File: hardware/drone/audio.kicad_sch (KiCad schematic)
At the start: 0 parts

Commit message: Worked on audio schematic (Codec, mic, d class audio amp, speaker)
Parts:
- added C66, C70, C71, C75, C76, C77: 100n, symbol Device:C
- added C67, C69, C72, C79: 10u, symbol Device:C
- added C68, C73, C74, C78: 1u, symbol Device:C
- added LS1: Speaker, symbol Device:Speaker
- added MK2: IM73A135V01, Sensor_Audio:Infineon_PG-LLGA-5-2, symbol Sensor_Audio:IM73A135V01
- added R10, R9: 150k, symbol Device:R
- added U11: TAC5111, Package_SO:SOIC-8_3.9x4.9mm_P1.27mm, symbol SoftDrone:TAC5111
- added U12: LM4670SD/NOPB, Package_TO_SOT_SMD:SOT-23-5, symbol SoftDrone:LM4670SD/NOPB
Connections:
- new net: C69.1, C70.1, U11.1 (DREG)
- new net: C73.2, U11.15 (IN1P)
- new net: C74.2, U11.16 (IN1M)
- new net: C76.1, U11.19 (OUT1P)
- new net: C77.2, U11.20 (OUT1M)
- new net: C68.1, U11.24 (VREF)
- new net: C76.2, R9.1
- new net: R9.2, U12.2 (-IN)
- new net: C73.1, MK2.1 (OUT+)
- new net: C77.1, R10.1
- new net: LS1.1, U12.8 (VO2)
- new net: LS1.2, U12.5 (VO1)
- new net: R10.2, U12.3 (+IN)
- new net: C74.1, MK2.3 (OUT-)
- new net GND: C66.2, C67.2, C68.2, C69.2, C70.2, C71.2, C72.2, C75.1, C78.2, C79.2, MK2.4 (GND), MK2.5 (GND), U11.13 (ADDR), U11.25 (VSS), U11.26 (VSS), U11.27 (VSS), U11.28 (VSS), U11.29 (VSS), U12.4 (GND), U12.6 (GND), U12.9 (EP)
- new net VDD1V8: C71.1, C72.1, U11.6 (IOVDD)
- new net VDD2V75: C75.2, MK2.2 (V_{DD})
- new net VDD3V3: C66.1, C67.1, U11.23 (AVDD)
- new net VSYS_5V: C78.1, C79.1, U12.7 (VDD)

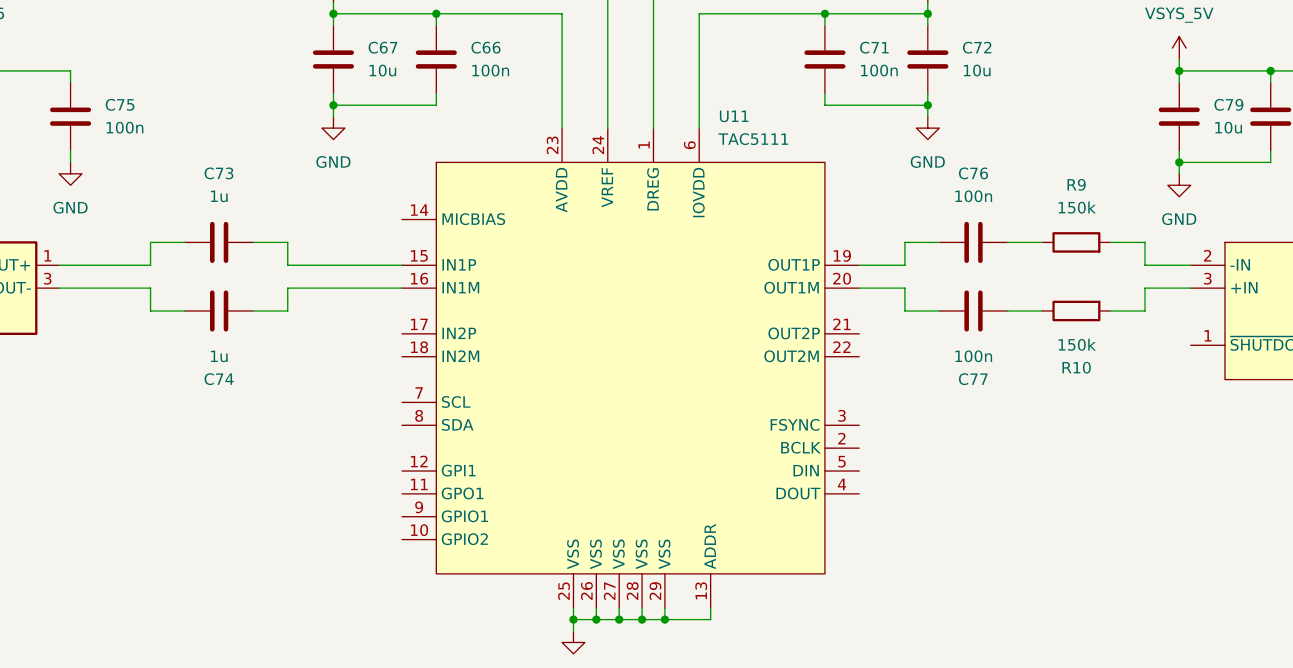
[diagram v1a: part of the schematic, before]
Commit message: Pinmuxxed codec and picked and completed IMU schematic
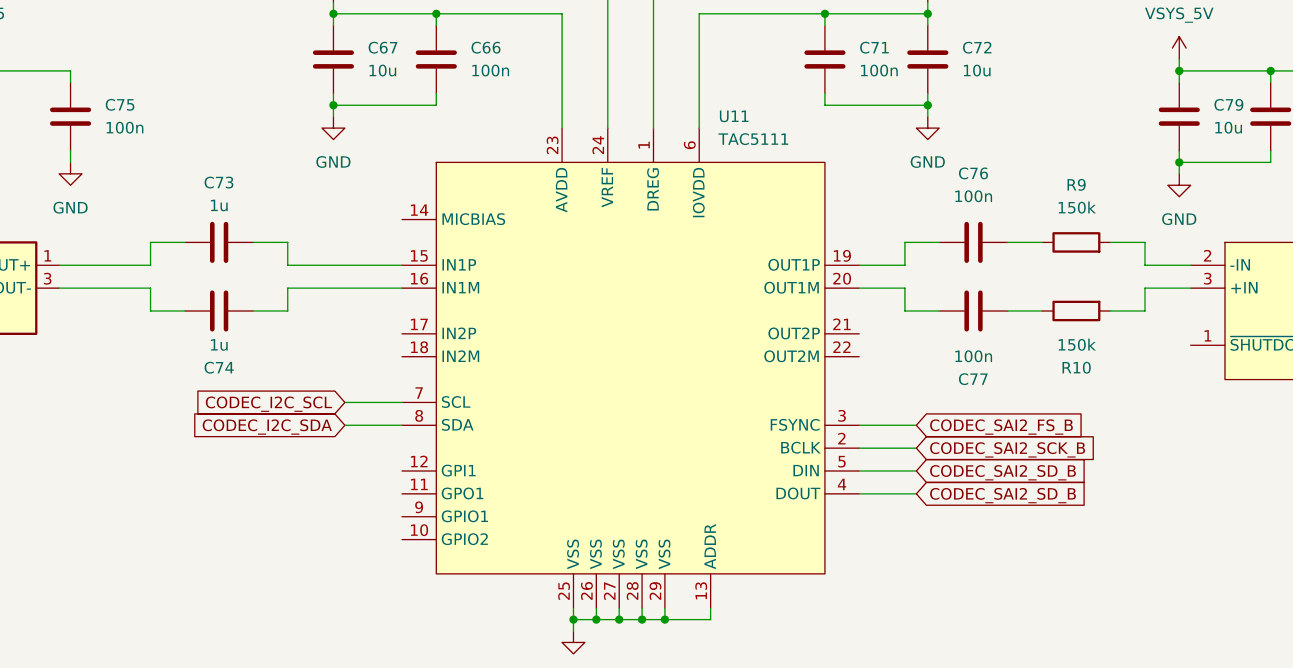
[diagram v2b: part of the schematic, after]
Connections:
- net CODEC_SAI2_SCK_B: now reaches U11.2 (BCLK)
- net CODEC_SAI2_FS_B: now reaches U11.3 (FSYNC)
- net CODEC_SAI2_SD_B: now reaches U11.4 (DOUT)
- net CODEC_SAI2_SD_B: now also U11.5 (DIN)
- net CODEC_I2C_SCL: now reaches U11.7 (SCL)
- net CODEC_I2C_SDA: now reaches U11.8 (SDA)
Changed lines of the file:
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@@
 	(wire
 		(pts
+			(xy 96.52 96.52) (xy 102.87 96.52)
+		)
+		(stroke
+			(width 0)
+			(type default)
+		)
+	)
+	(wire
+		(pts
 			(xy 189.23 69.85) (xy 199.39 69.85)
 		)
@@
 	(wire
 		(pts
+			(xy 96.52 99.06) (xy 102.87 99.06)
+		)
+		(stroke
+			(width 0)
+			(type default)
+		)
+	)
+	(wire
+		(pts
 			(xy 74.93 83.82) (xy 64.77 83.82)
 		)
@@
 	(wire
 		(pts
+			(xy 160.02 106.68) (xy 153.67 106.68)
+		)
+		(stroke
+			(width 0)
+			(type default)
+		)
+	)
+	(wire
+		(pts
 			(xy 199.39 60.96) (xy 199.39 59.69)
 		)
@@
 	(wire
 		(pts
+			(xy 160.02 104.14) (xy 153.67 104.14)
+		)
+		(stroke
+			(width 0)
+			(type default)
+		)
+	)
+	(wire
+		(pts
 			(xy 228.6 81.28) (xy 234.95 81.28)
 		)
@@
 	(wire
 		(pts
+			(xy 160.02 99.06) (xy 153.67 99.06)
+		)
+		(stroke
+			(width 0)
+			(type default)
+		)
+	)
+	(wire
+		(pts
 			(xy 189.23 71.12) (xy 189.23 69.85)
 		)
@@
 	(wire
 		(pts
+			(xy 160.02 101.6) (xy 153.67 101.6)
+		)
+		(stroke
+			(width 0)
+			(type default)
+		)
+	)
+	(wire
+		(pts
 			(xy 129.54 120.65) (xy 127 120.65)
 		)
@@
 		)
 	)
+	(global_label "CODEC_SAI2_SD_B"
+		(shape input)
+		(at 160.02 104.14 0)
+		(fields_autoplaced yes)
+		(effects
+			(font
+				(size 1.27 1.27)
+			)
+			(justify left)
+		)
+		(property "Intersheetrefs" "${INTERSHEET_REFS}"
+			(at 180.0594 104.14 0)
+			(hide yes)
+			(show_name no)
+			(do_not_autoplace no)
+			(effects
+				(font
+					(size 1.27 1.27)
+				)
+				(justify left)
+			)
+		)
+	)
+	(global_label "CODEC_I2C_SDA"
+		(shape input)
+		(at 96.52 99.06 180)
+		(fields_autoplaced yes)
+		(effects
+			(font
+				(size 1.27 1.27)
+			)
+			(justify right)
+		)
+		(property "Intersheetrefs" "${INTERSHEET_REFS}"
+			(at 78.6577 99.06 0)
+			(hide yes)
+			(show_name no)
+			(do_not_autoplace no)
+			(effects
+				(font
+					(size 1.27 1.27)
+				)
+				(justify right)
+			)
+		)
+	)
+	(global_label "CODEC_SAI2_SCK_B"
+		(shape input)
+		(at 160.02 101.6 0)
+		(fields_autoplaced yes)
+		(effects
+			(font
+				(size 1.27 1.27)
+			)
+			(justify left)
+		)
+		(property "Intersheetrefs" "${INTERSHEET_REFS}"
+			(at 179.878 101.6 0)
+			(hide yes)
+			(show_name no)
+			(do_not_autoplace no)
+			(effects
+				(font
+					(size 1.27 1.27)
+				)
+				(justify left)
+			)
+		)
+	)
+	(global_label "CODEC_SAI2_FS_B"
+		(shape input)
+		(at 160.02 99.06 0)
+		(fields_autoplaced yes)
+		(effects
+			(font
+				(size 1.27 1.27)
+			)
+			(justify left)
+		)
+		(property "Intersheetrefs" "${INTERSHEET_REFS}"
+			(at 181.3294 99.06 0)
+			(hide yes)
+			(show_name no)
+			(do_not_autoplace no)
+			(effects
+				(font
+					(size 1.27 1.27)
+				)
+				(justify left)
+			)
+		)
+	)
+	(global_label "CODEC_SAI2_SD_B"
+		(shape input)
+		(at 160.02 106.68 0)
+		(fields_autoplaced yes)
+		(effects
+			(font
+				(size 1.27 1.27)
+			)
+			(justify left)
+		)
+		(property "Intersheetrefs" "${INTERSHEET_REFS}"
+			(at 180.0594 106.68 0)
+			(hide yes)
+			(show_name no)
+			(do_not_autoplace no)
+			(effects
+				(font
+					(size 1.27 1.27)
+				)
+				(justify left)
+			)
+		)
+	)
+	(global_label "CODEC_I2C_SCL"
+		(shape input)
+		(at 96.52 96.52 180)
+		(fields_autoplaced yes)
+		(effects
+			(font
+				(size 1.27 1.27)
+			)
+			(justify right)
+		)
+		(property "Intersheetrefs" "${INTERSHEET_REFS}"
+			(at 78.7182 96.52 0)
+			(hide yes)
+			(show_name no)
+			(do_not_autoplace no)
+			(effects
+				(font
+					(size 1.27 1.27)
+				)
+				(justify right)
+			)
+		)
+	)
 	(symbol
 		(lib_id "power:VDD")
@@
 		(in_pos_files yes)
 		(dnp no)
-		(fields_autoplaced yes)
 		(property "Reference" "C73"
-			(at 82.55 71.12 90)
+			(at 82.55 72.136 90)
 			(show_name no)
 			(do_not_autoplace no)
@@
 		)
 		(property "Value" "1u"
-			(at 82.55 73.66 90)
+			(at 82.55 74.676 90)
 			(show_name no)
 			(do_not_autoplace no)
@@
 		(dnp no)
 		(property "Reference" "C74"
-			(at 82.55 93.98 90)
+			(at 82.55 92.71 90)
 			(show_name no)
 			(do_not_autoplace no)
@@
 		)
 		(property "Value" "1u"
-			(at 82.55 91.44 90)
+			(at 82.55 90.17 90)
 			(show_name no)
 			(do_not_autoplace no)

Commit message: Finished GNSS, did more pinmuxxing
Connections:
- net CODEC_IRQ: now reaches U11.9 (GPIO1)
- net CODEC_I2C_SCL renamed CODEC_I2C2_SCL
- net CODEC_I2C_SDA renamed CODEC_I2C2_SDA
- no-connect marks 0 -> 7
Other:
- note added: "Audio Codec"
- moved on the sheet: C66, C67, C68, C69, C70, C71, C72, C73, C74, C75, C76, C77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

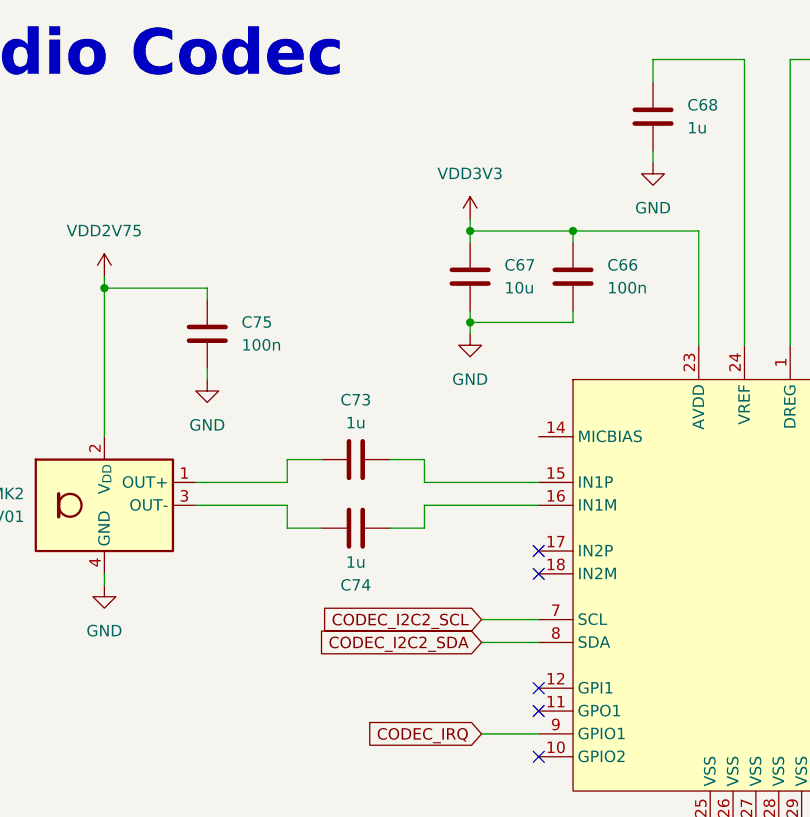
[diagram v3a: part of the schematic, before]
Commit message: Added barometer, more pinmuxxing, added VBAT sensing and reverse voltage protection
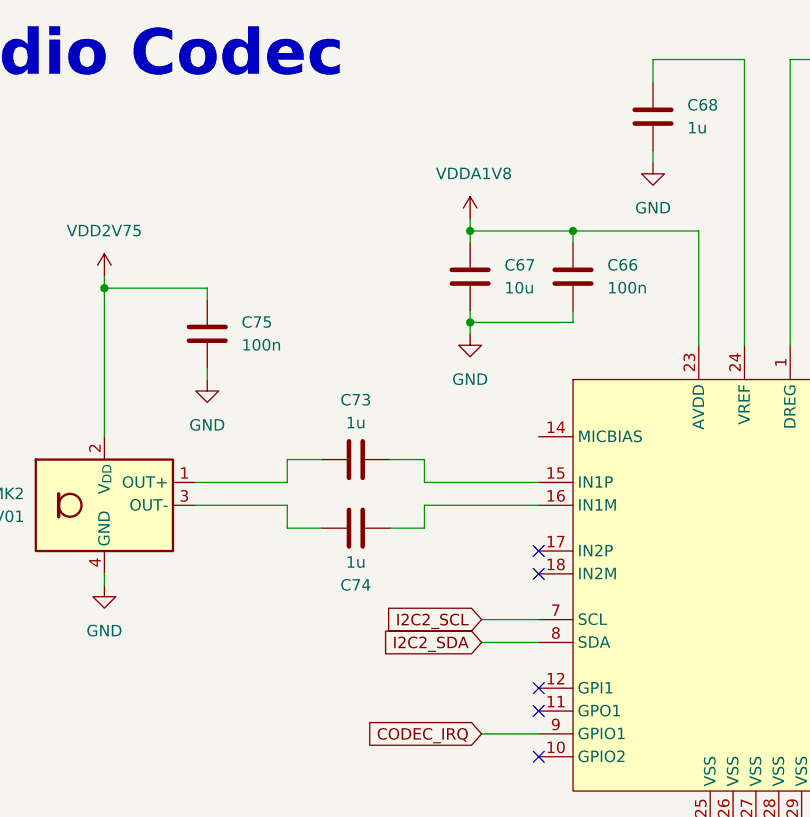
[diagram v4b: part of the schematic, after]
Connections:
- net CODEC_I2C2_SCL renamed I2C2_SCL
- net CODEC_I2C2_SDA renamed I2C2_SDA
- net VDD3V3 renamed VDDA1V8
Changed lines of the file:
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@@
 		)
 	)
-	(global_label "CODEC_I2C2_SDA"
+	(global_label "I2C2_SDA"
 		(shape input)
 		(at 91.44 97.79 180)
@@
 		)
 		(property "Intersheetrefs" "${INTERSHEET_REFS}"
-			(at 72.3682 97.79 0)
+			(at 79.6253 97.79 0)
 			(hide yes)
 			(show_name no)
@@
 		)
 	)
-	(global_label "CODEC_I2C2_SCL"
+	(global_label "I2C2_SCL"
 		(shape input)
 		(at 91.44 95.25 180)
@@
 		)
 		(property "Intersheetrefs" "${INTERSHEET_REFS}"
-			(at 72.4287 95.25 0)
+			(at 79.6858 95.25 0)
 			(hide yes)
 			(show_name no)
@@
 		(in_pos_files yes)
 		(dnp no)
-		(fields_autoplaced yes)
 		(property "Reference" "#PWR093"
 			(at 90.17 54.61 0)
@@
 			)
 		)
-		(property "Value" "VDD3V3"
-			(at 90.17 45.72 0)
-			(show_name no)
-			(do_not_autoplace no)
-			(effects
-				(font
-					(size 1.27 1.27)
-				)
-			)
-		)
+		(property "Value" "VDDA1V8"
+			(at 86.36 45.72 0)
+			(show_name no)
+			(do_not_autoplace no)
+			(effects
+				(font
+					(size 1.27 1.27)
+				)
+				(justify left)
+			)
+		)

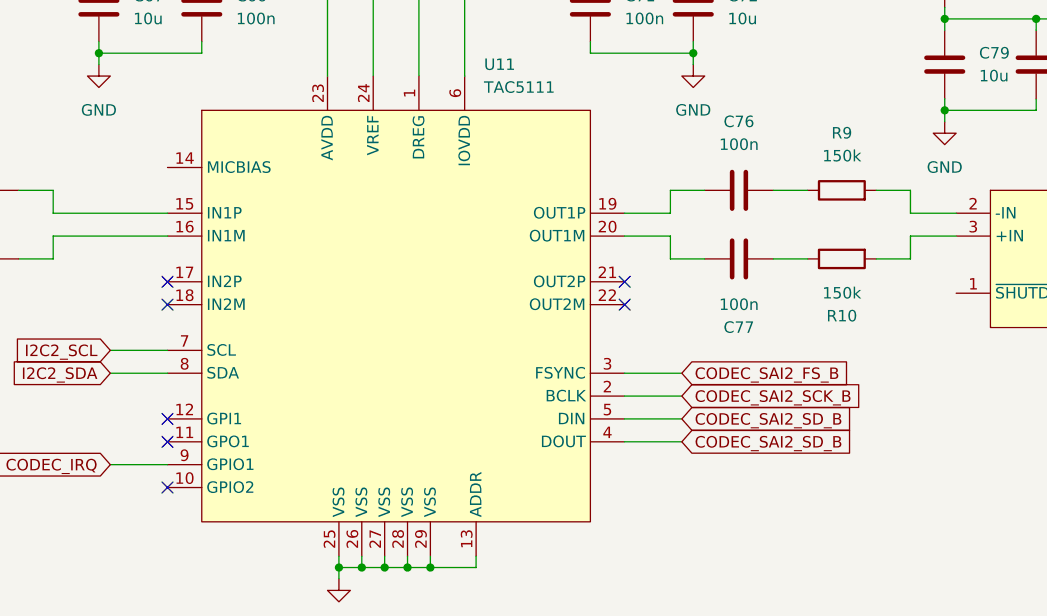
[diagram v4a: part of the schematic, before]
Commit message: Created pinmux table and completed pinmuxing
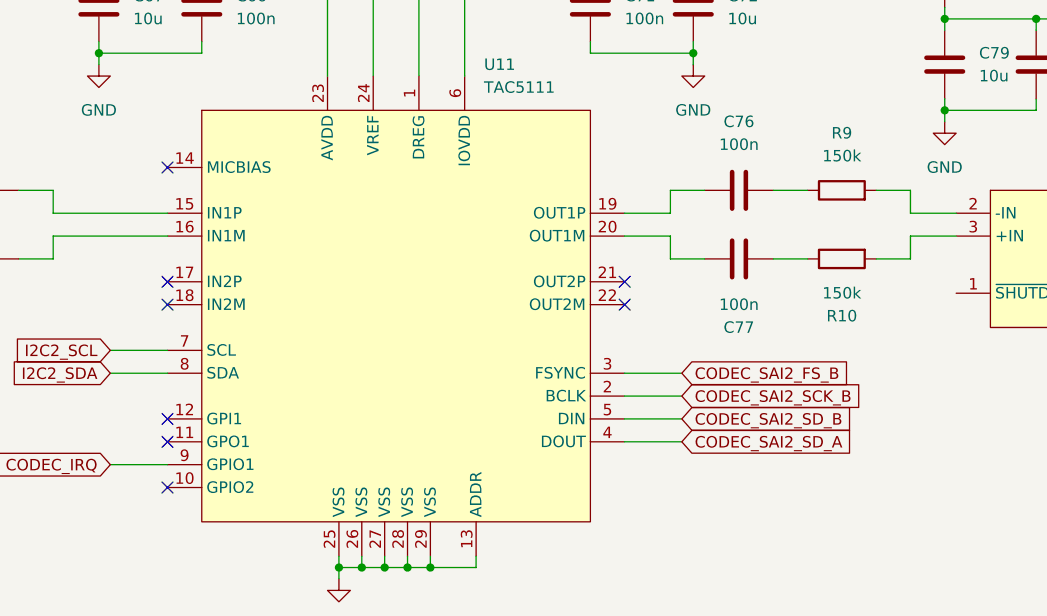
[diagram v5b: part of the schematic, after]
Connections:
- net CODEC_SAI2_SD_B: no longer U11.4 (DOUT)
- new net CODEC_SAI2_SD_A: U11.4 (DOUT)
- no-connect marks 7 -> 8
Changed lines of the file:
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@@
+	)
+	(no_connect
+		(at 97.79 74.93)
 	)
 	(no_connect
@@
 		)
 	)
-	(global_label "CODEC_SAI2_SD_B"
+	(global_label "CODEC_SAI2_SD_A"
 		(shape input)
 		(at 154.94 105.41 0)
@@
 		)
 		(property "Intersheetrefs" "${INTERSHEET_REFS}"
-			(at 174.9794 105.41 0)
+			(at 174.798 105.41 0)
 			(hide yes)
 			(show_name no)

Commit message: Small cleanup
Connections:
- net SPK_EN: now reaches U12.1 (~{SHUTDOWN})
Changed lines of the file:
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@@
+	(wire
+		(pts
+			(xy 182.88 88.9) (xy 185.42 88.9)
+		)
+		(stroke
+			(width 0)
+			(type default)
+		)
+	)
 	(wire
 		(pts
@@
 		(property "Intersheetrefs" "${INTERSHEET_REFS}"
 			(at 79.6858 95.25 0)
+			(hide yes)
+			(show_name no)
+			(do_not_autoplace no)
+			(effects
+				(font
+					(size 1.27 1.27)
+				)
+				(justify right)
+			)
+		)
+	)
+	(global_label "SPK_EN"
+		(shape input)
+		(at 182.88 88.9 180)
+		(fields_autoplaced yes)
+		(effects
+			(font
+				(size 1.27 1.27)
+			)
+			(justify right)
+		)
+		(property "Intersheetrefs" "${INTERSHEET_REFS}"
+			(at 172.6982 88.9 0)
 			(hide yes)
 			(show_name no)
@@
 		(in_pos_files yes)
 		(dnp no)
-		(fields_autoplaced yes)
 		(property "Reference" "R9"
-			(at 172.72 71.12 90)
+			(at 172.72 74.93 90)
 			(show_name no)
 			(do_not_autoplace no)
@@
 		)
 		(property "Value" "150k"
-			(at 172.72 73.66 90)
+			(at 172.72 77.47 90)
 			(show_name no)
 			(do_not_autoplace no)
@@
 		(dnp no)
 		(property "Reference" "R10"
-			(at 172.72 91.44 90)
+			(at 172.72 82.55 90)
 			(show_name no)
 			(do_not_autoplace no)
@@
 		)
 		(property "Value" "150k"
-			(at 172.72 88.9 90)
-			(show_name no)
-			(do_not_autoplace no)
+			(at 172.72 85.09 90)
+			(show_name no)
+			(do_not_autoplace no)

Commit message: Started footprint assignments
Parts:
- U11: value TAC5111 -> TAC5111IRGER; footprint Package_SO:SOIC-8_3.9x4.9mm_P1.27mm -> SoftDroneLibrary:TAC5111IRGER
- U12: footprint Package_TO_SOT_SMD:SOT-23-5 -> (none)
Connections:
- net GND: now also U11.A1 (VSS), U11.A2 (VSS), U11.A3 (VSS), U11.A4 (VSS); no longer U11.26 (VSS), U11.27 (VSS), U11.28 (VSS), U11.29 (VSS)
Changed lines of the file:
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@@
 			)
 		)
-		(property "Value" "TAC5111"
+		(property "Value" "TAC5111IRGER"
 			(at 132.9533 66.04 0)
 			(show_name no)
@@
 			)
 		)
-		(property "Footprint" "Package_SO:SOIC-8_3.9x4.9mm_P1.27mm"
+		(property "Footprint" "SoftDroneLibrary:TAC5111IRGER"
 			(at 123.19 91.44 0)
 			(hide yes)
@@
 		(pin "15"
 		)
-		(pin "28"
+		(pin "A4"
 		)
 		(pin "20"
 		)
-		(pin "26"
+		(pin "A1"
 		)
 		(pin "2"
@@
 		(pin "8"
 		)
-		(pin "29"
-		)
-		(pin "27"
+		(pin "A2"
+		)
+		(pin "A3"
 		)
 		(pin "9"
@@
 			)
 		)
-		(property "Footprint" "Package_TO_SOT_SMD:SOT-23-5"
+		(property "Footprint" ""
 			(at 204.47 85.09 0)
 			(hide yes)

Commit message: Continued footprint assignments
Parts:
- U12: footprint (none) -> Package_SON:WSON-8-1EP_3x3mm_P0.5mm_EP1.6x2.0mm
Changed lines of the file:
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@@
 			)
 		)
-		(property "Footprint" ""
+		(property "Footprint" "Package_SON:WSON-8-1EP_3x3mm_P0.5mm_EP1.6x2.0mm"
 			(at 204.47 85.09 0)
 			(hide yes)
